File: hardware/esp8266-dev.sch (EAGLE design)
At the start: 31 parts, among them CON1 USBB-SOCKET, J1 AVR_SPI_PRG_6PTH

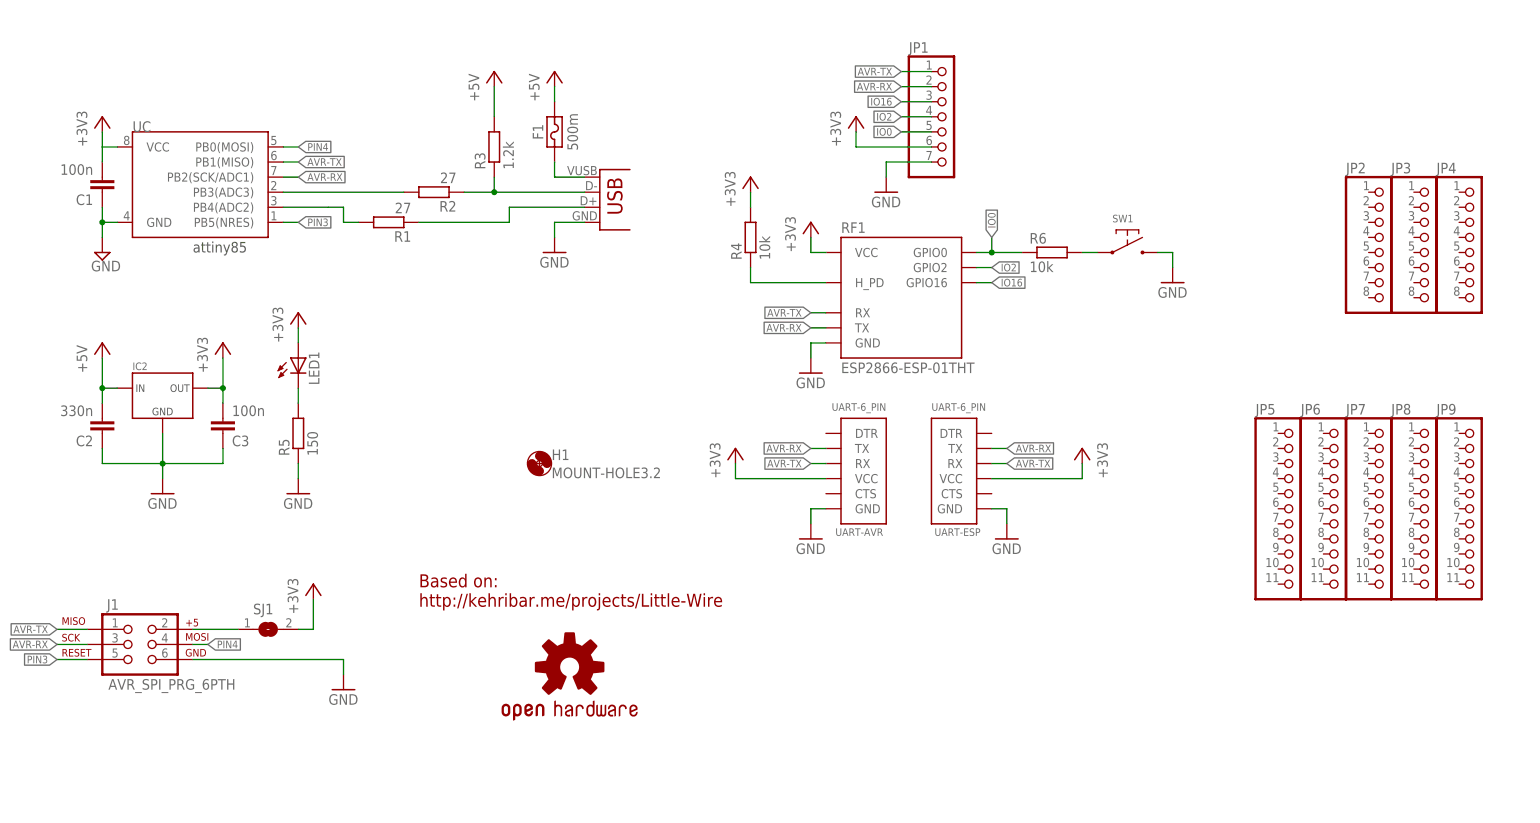
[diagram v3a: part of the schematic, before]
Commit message: basic lazyout done, cleaning up silkscreen
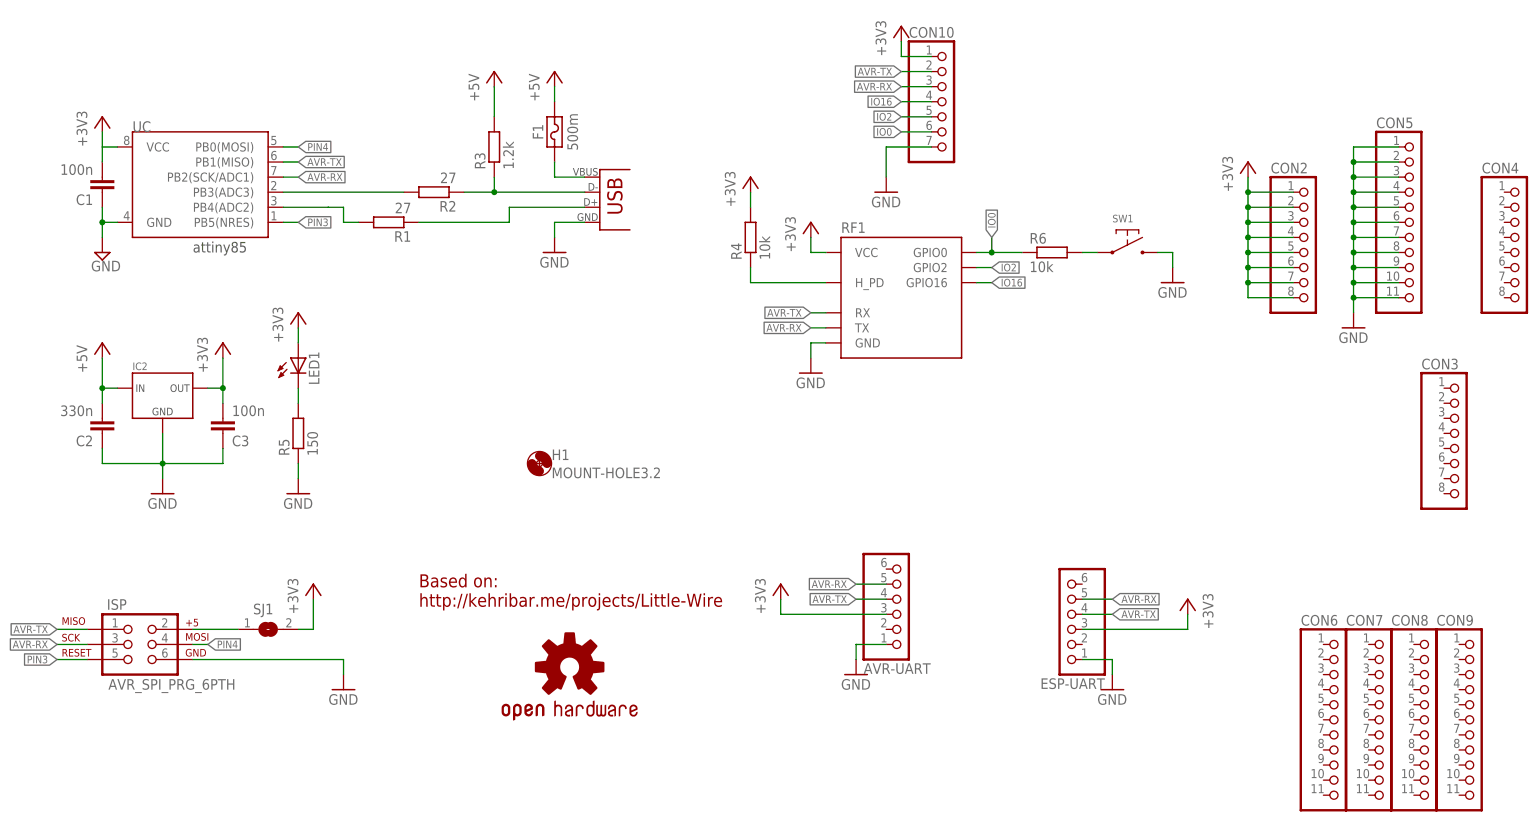
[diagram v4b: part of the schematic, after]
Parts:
- removed JP1: (no value), pinhead:PINHD-1X7
- removed JP2, JP3, JP4: (no value), pinhead:PINHD-1X8
- removed JP5, JP6, JP7, JP8, JP9: (no value), pinhead:PINHD-1X11
- removed UART-AVR, UART-ESP: UART-6_PIN, p.peter-connectors:UART-6_PIN
- added AVR-UART, ESP-UART: (no value), p.peter-connectors:GENERIC-1X6STANDARD
- added CON10: (no value), p.peter-connectors:GENERIC-1X7NOSILK
- added CON2, CON3, CON4: (no value), p.peter-connectors:GENERIC-1X8NOSILK
- added CON5, CON6, CON7, CON8, CON9: (no value), p.peter-connectors:GENERIC-1X11NOSILK
- RF1: value ESP2866-ESP-01THT -> (none); device p.peter-periphery:ESP2866-ESP-01THT -> p.peter-periphery:ESP2866-ESP-01THT-NOSILK
- UC: value ATTINY45DIP8 -> ATTINY85
- renumbered J1 to ISP
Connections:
- net N$5 renamed D-
- net +3V3: now also AVR-UART.3, CON10.1, CON2.1, CON2.2, CON2.3, CON2.4, CON2.5, CON2.6, CON2.7, CON2.8, ESP-UART.3; no longer JP1.6, UART-AVR.VCC, UART-ESP.VCC
- net AVR-RX: now also AVR-UART.5, CON10.3, ESP-UART.5; no longer JP1.2, UART-AVR.TX, UART-ESP.TX
- net AVR-TX: now also AVR-UART.4, CON10.2, ESP-UART.4; no longer JP1.1, UART-AVR.RX, UART-ESP.RX
- net GND: now also AVR-UART.1, CON10.7, CON5.1, CON5.10, CON5.11, CON5.2, CON5.3, CON5.4, CON5.5, CON5.6, CON5.7, CON5.8, CON5.9, ESP-UART.1; no longer JP1.7, UART-AVR.GND, UART-ESP.GND
- net IO0: now also CON10.6; no longer JP1.5
- net IO16: now also CON10.4; no longer JP1.3
- net IO2: now also CON10.5; no longer JP1.4

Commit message: Further cleanup
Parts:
- IC2: value (none) -> 3V3
- R1, R2: value 27 -> 68
- R3: value 1.2k -> 1.5k
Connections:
- net +3V3: now also R3.2
- net +5V: no longer R3.2
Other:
- moved on the sheet: CON10, CON2, CON3, CON4, CON6, CON7, CON8, CON9, ESP-UART, H1, R4, R6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

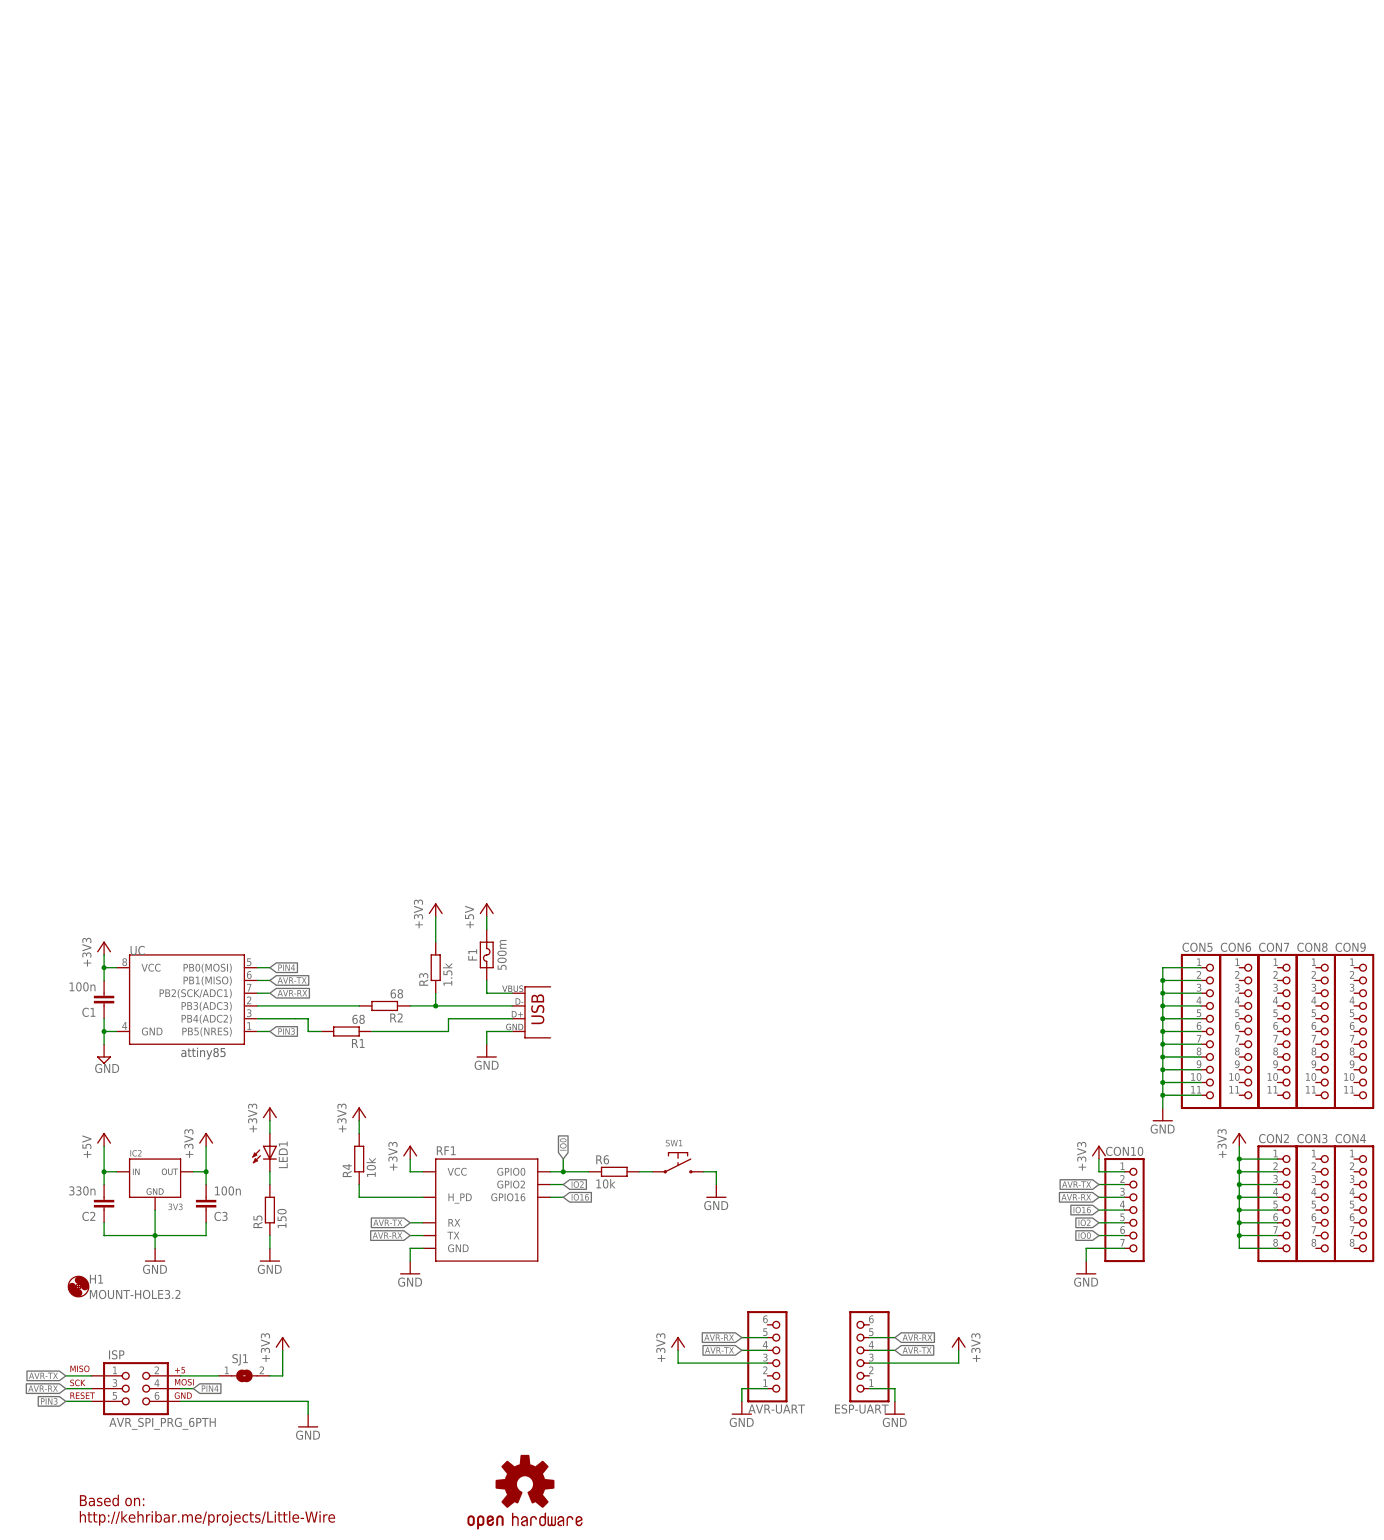
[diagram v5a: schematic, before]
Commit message: Cleaned up schematic
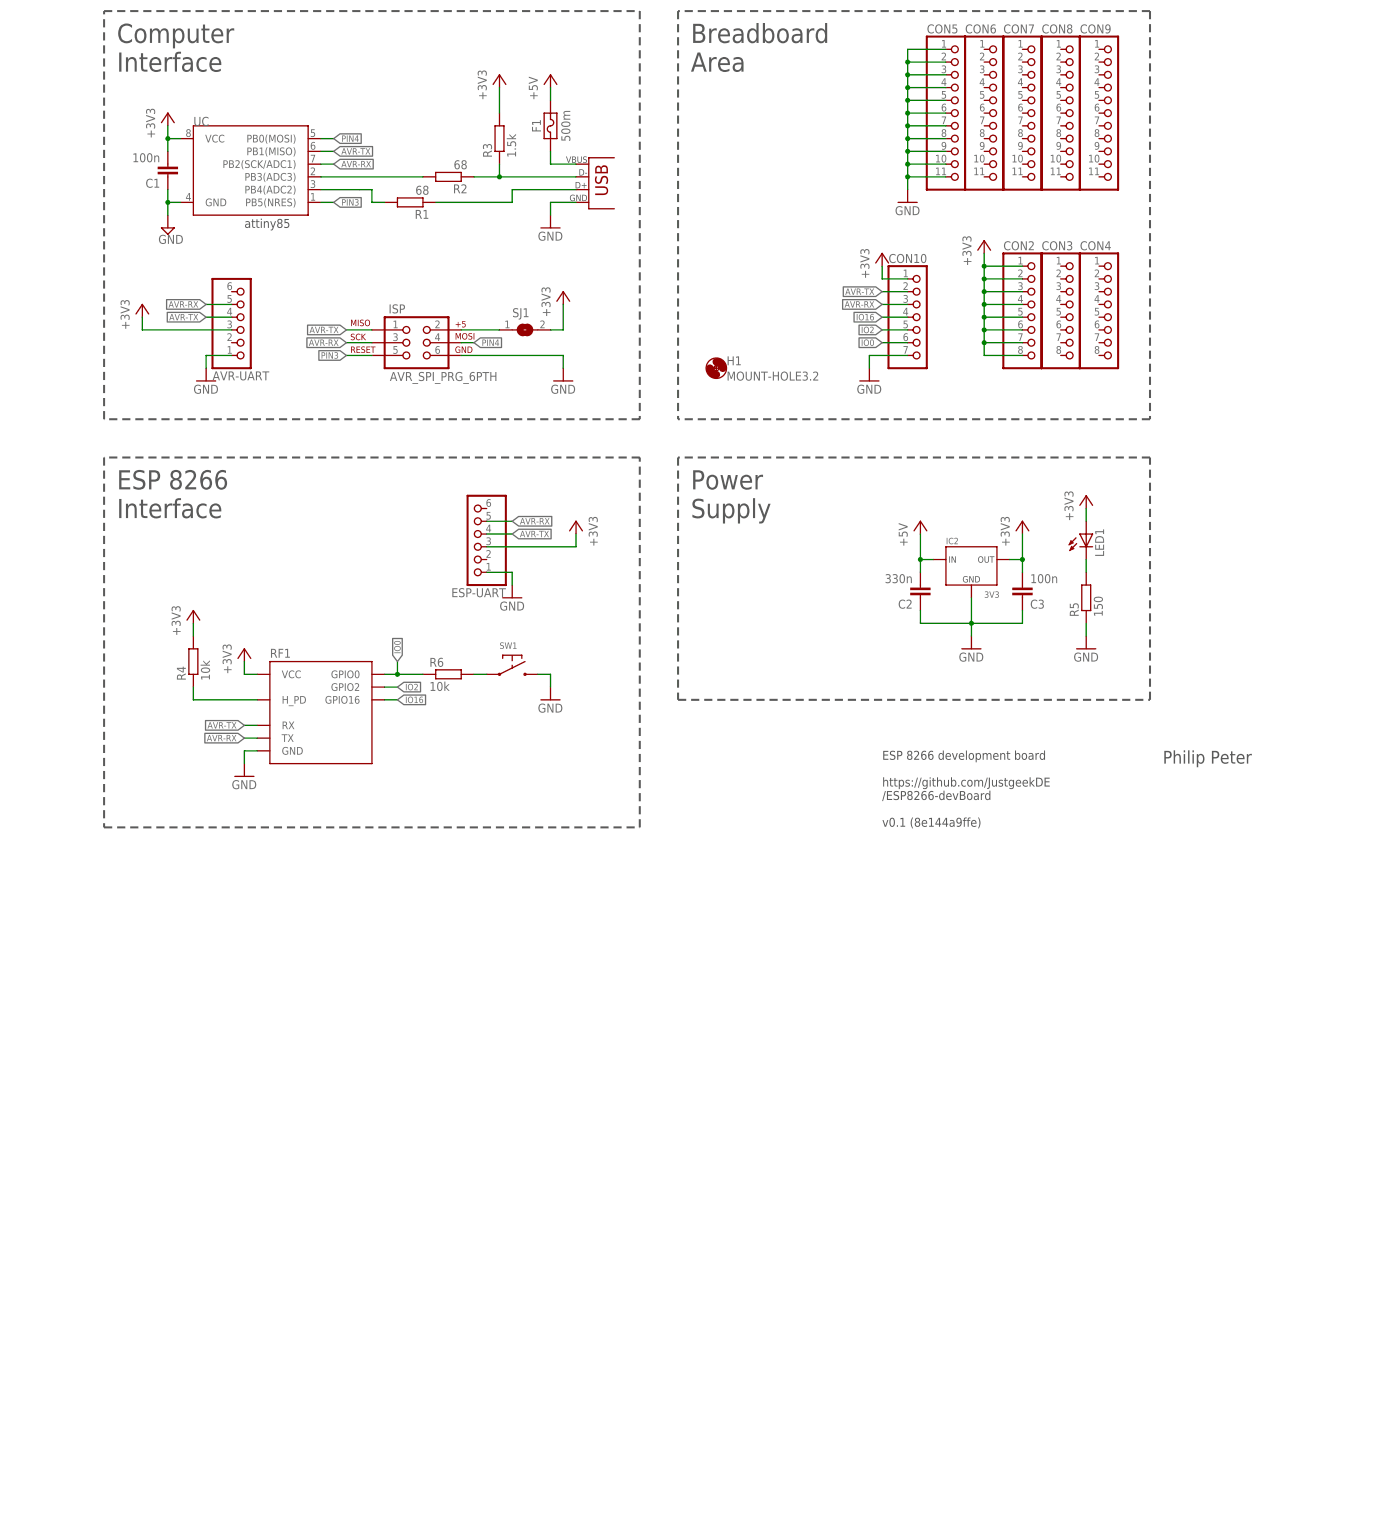
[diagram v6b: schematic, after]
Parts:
- removed U$1: OSHW-LOGOS, SparkFun:OSHW-LOGOS
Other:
- note added: "Breadboard Area"
- note added: "Computer Interface"
- note added: "ESP 8266 Interface"
- note added: "ESP 8266 development board https://github.com/JustgeekDE /ESP8266-devBoard v0.1 (8e144a9ffe)"
- note added: "Philip Peter"
- note added: "Power Supply"
- note removed: "Based on: http://kehribar.me/projects/Little-Wire"
- moved on the sheet: AVR-UART, C1, C2, C3, CON10, CON2, CON3, CON4, CON5, CON6, CON7, CON8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
